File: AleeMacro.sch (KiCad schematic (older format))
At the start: 50 parts, among them J1 Conn_01x04_Male (OLED), SW1 SW_Push, U1 ProMicro

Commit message: Routing Adjustments
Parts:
- renumbered MX15a to MX16a1, MX19 to MX18a1
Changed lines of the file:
@@
 EESchema Schematic File Version 4
+LIBS:AleeMacro-cache
 EELAYER 30 0
 EELAYER END
@@
 	8525 5175 7925 5175
 $Comp
-L MX_Alps_Hybrids:MX-1U MX19
+L MX_Alps_Hybrids:MX-1U MX18a1
 U 1 1 5C43AB0B
 P 9725 4800
-F 0 "MX19" H 9811 5017 60  0000 C CNN
+F 0 "MX18a1" H 9811 5017 60  0000 C CNN
 F 1 "MX-2U" H 9811 4943 20  0000 C CNN
 F 2 "MX_Alps_Hybrid:MX-2U-ReversedStabilizers-NoLED" H 9700 4775 60  0001 C CNN
@@
 $EndComp
 $Comp
-L MX_Alps_Hybrids:MX-1U MX15a
+L MX_Alps_Hybrids:MX-1U MX16a1
 U 1 1 5C43B474
 P 8025 5550
-F 0 "MX15a" H 8111 5767 60  0000 C CNN
+F 0 "MX16a1" H 8111 5767 60  0000 C CNN
 F 1 "MX-2U" H 8111 5693 20  0000 C CNN
 F 2 "MX_Alps_Hybrid:MX-2U-ReversedStabilizers-NoLED" H 8000 5525 60  0001 C CNN

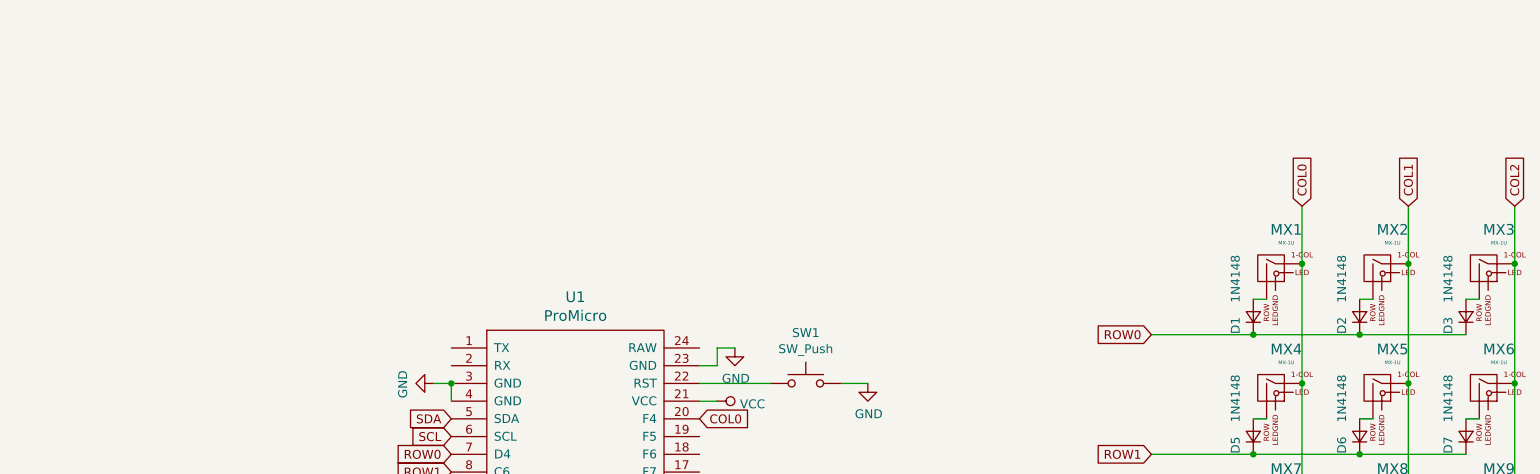
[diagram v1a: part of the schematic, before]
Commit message: LEDS added
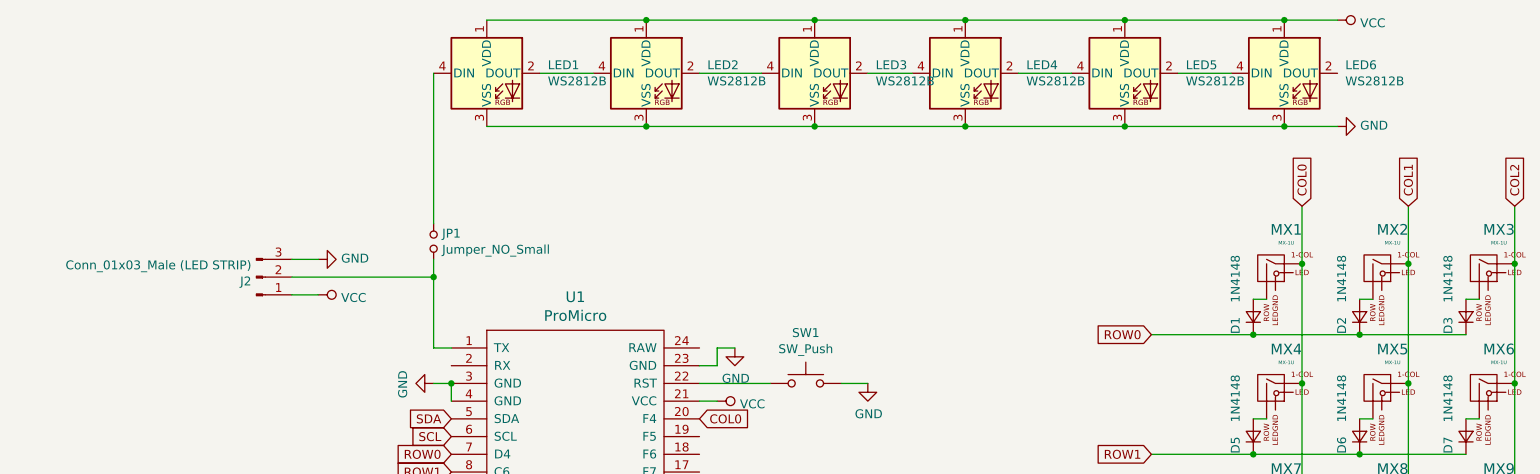
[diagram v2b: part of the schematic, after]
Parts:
- added J2: Conn_01x03_Male (LED STRIP), Connector_PinHeader_2.54mm:PinHeader_1x03_P2.54mm_Vertical, symbol Connector:Conn_01x03_Male
- added JP1: Jumper_NO_Small, Jumper:SolderJumper-2_P1.3mm_Open_Pad1.0x1.5mm, symbol Device:Jumper_NO_Small
- added LED1, LED2, LED3, LED4, LED5, LED6: WS2812B, LED_SMD:LED_WS2812B_PLCC4_5.0x5.0mm_P3.2mm, symbol LED:WS2812B
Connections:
- net GND: now also J2.3 (Pin_3), LED1.3 (VSS), LED2.3 (VSS), LED3.3 (VSS), LED4.3 (VSS), LED5.3 (VSS), LED6.3 (VSS)
- net VCC: now also J2.1 (Pin_1), LED1.1 (VDD), LED2.1 (VDD), LED3.1 (VDD), LED4.1 (VDD), LED5.1 (VDD), LED6.1 (VDD)
- net at U1.1 (TX): now also J2.2 (Pin_2), JP1.2
- new net: LED1.2 (DOUT), LED2.4 (DIN)
- new net: JP1.1, LED1.4 (DIN)
- new net: LED2.2 (DOUT), LED3.4 (DIN)
- new net: LED3.2 (DOUT), LED4.4 (DIN)
- new net: LED4.2 (DOUT), LED5.4 (DIN)
- new net: LED5.2 (DOUT), LED6.4 (DIN)
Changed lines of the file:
@@
 Wire Wire Line
 	4200 2850 4300 2850
+$Comp
+L power:GND #PWR0109
+U 1 1 6125BC2F
+P 7800 1300
+F 0 "#PWR0109" H 7800 1050 50  0001 C CNN
+F 1 "GND" V 7805 1172 50  0000 R CNN
+F 2 "" H 7800 1300 50  0001 C CNN
+F 3 "" H 7800 1300 50  0001 C CNN
+	1    7800 1300
+	0    -1   -1   0
+$EndComp
+$Comp
+L LED:WS2812B LED1
+U 1 1 61219799
+P 3000 1000
+F 0 "LED1" H 3344 1046 50  0000 L CNN
+F 1 "WS2812B" H 3344 955 50  0000 L CNN
+F 2 "LED_SMD:LED_WS2812B_PLCC4_5.0x5.0mm_P3.2mm" H 3050 700 50  0001 L TNN
+F 3 "https://cdn-shop.adafruit.com/datasheets/WS2812B.pdf" H 3100 625 50  0001 L TNN
+	1    3000 1000
+	1    0    0    -1
+$EndComp
+Wire Wire Line
+	2700 2550 2800 2550
+$Comp
+L LED:WS2812B LED4
+U 1 1 61284E59
+P 5700 1000
+F 0 "LED4" H 6044 1046 50  0000 L CNN
+F 1 "WS2812B" H 6044 955 50  0000 L CNN
+F 2 "LED_SMD:LED_WS2812B_PLCC4_5.0x5.0mm_P3.2mm" H 5750 700 50  0001 L TNN
+F 3 "https://cdn-shop.adafruit.com/datasheets/WS2812B.pdf" H 5800 625 50  0001 L TNN
+	1    5700 1000
+	1    0    0    -1
+$EndComp
+$Comp
+L LED:WS2812B LED5
+U 1 1 612874EB
+P 6600 1000
+F 0 "LED5" H 6944 1046 50  0000 L CNN
+F 1 "WS2812B" H 6944 955 50  0000 L CNN
+F 2 "LED_SMD:LED_WS2812B_PLCC4_5.0x5.0mm_P3.2mm" H 6650 700 50  0001 L TNN
+F 3 "https://cdn-shop.adafruit.com/datasheets/WS2812B.pdf" H 6700 625 50  0001 L TNN
+	1    6600 1000
+	1    0    0    -1
+$EndComp
+$Comp
+L LED:WS2812B LED6
+U 1 1 61289AF9
+P 7500 1000
+F 0 "LED6" H 7844 1046 50  0000 L CNN
+F 1 "WS2812B" H 7844 955 50  0000 L CNN
+F 2 "LED_SMD:LED_WS2812B_PLCC4_5.0x5.0mm_P3.2mm" H 7550 700 50  0001 L TNN
+F 3 "https://cdn-shop.adafruit.com/datasheets/WS2812B.pdf" H 7600 625 50  0001 L TNN
+	1    7500 1000
+	1    0    0    -1
+$EndComp
+Wire Wire Line
+	3300 1000 3600 1000
+Wire Wire Line
+	3000 1300 3900 1300
+$Comp
+L LED:WS2812B LED2
+U 1 1 6122436D
+P 3900 1000
+F 0 "LED2" H 4244 1046 50  0000 L CNN
+F 1 "WS2812B" H 4244 955 50  0000 L CNN
+F 2 "LED_SMD:LED_WS2812B_PLCC4_5.0x5.0mm_P3.2mm" H 3950 700 50  0001 L TNN
+F 3 "https://cdn-shop.adafruit.com/datasheets/WS2812B.pdf" H 4000 625 50  0001 L TNN
+	1    3900 1000
+	1    0    0    -1
+$EndComp
+$Comp
+L power:VCC #PWR0110
+U 1 1 61255F21
+P 7800 700
+F 0 "#PWR0110" H 7800 550 50  0001 C CNN
+F 1 "VCC" V 7817 828 50  0000 L CNN
+F 2 "" H 7800 700 50  0001 C CNN
+F 3 "" H 7800 700 50  0001 C CNN
+	1    7800 700
+	0    1    1    0
+$EndComp
+Wire Wire Line
+	3000 700  3900 700
+Connection ~ 3900 700
+Wire Wire Line
+	5700 700  6600 700
+Connection ~ 5700 700
+Wire Wire Line
+	6600 700  7500 700
+Connection ~ 6600 700
+Wire Wire Line
+	7500 700  7800 700
+Connection ~ 7500 700
+$Comp
+L LED:WS2812B LED3
+U 1 1 6128279B
+P 4850 1000
+F 0 "LED3" H 5194 1046 50  0000 L CNN
+F 1 "WS2812B" H 5194 955 50  0000 L CNN
+F 2 "LED_SMD:LED_WS2812B_PLCC4_5.0x5.0mm_P3.2mm" H 4900 700 50  0001 L TNN
+F 3 "https://cdn-shop.adafruit.com/datasheets/WS2812B.pdf" H 4950 625 50  0001 L TNN
+	1    4850 1000
+	1    0    0    -1
+$EndComp
+Wire Wire Line
+	3900 700  4850 700
+Connection ~ 4850 700
+Wire Wire Line
+	4850 700  5700 700
+Wire Wire Line
+	4200 1000 4550 1000
+Wire Wire Line
+	5150 1000 5400 1000
+Wire Wire Line
+	6000 1000 6300 1000
+Wire Wire Line
+	6900 1000 7200 1000
+Wire Wire Line
+	3900 1300 4850 1300
+Connection ~ 3900 1300
+Wire Wire Line
+	4850 1300 5700 1300
+Connection ~ 4850 1300
+Wire Wire Line
+	5700 1300 6600 1300
+Connection ~ 5700 1300
+Wire Wire Line
+	6600 1300 7500 1300
+Connection ~ 6600 1300
+Wire Wire Line
+	7500 1300 7800 1300
+Connection ~ 7500 1300
+$Comp
+L power:VCC #PWR0112
+U 1 1 612EDCFF
+P 2050 2250
+F 0 "#PWR0112" H 2050 2100 50  0001 C CNN
+F 1 "VCC" V 2067 2378 50  0000 L CNN
+F 2 "" H 2050 2250 50  0001 C CNN
+F 3 "" H 2050 2250 50  0001 C CNN
+	1    2050 2250
+	0    1    1    0
+$EndComp
+$Comp
+L Connector:Conn_01x03_Male J2
+U 1 1 612F1FD3
+P 1700 2150
+F 0 "J2" H 1672 2174 50  0000 R CNN
+F 1 "Conn_01x03_Male (LED STRIP)" H 1672 2083 50  0000 R CNN
+F 2 "Connector_PinHeader_2.54mm:PinHeader_1x03_P2.54mm_Vertical" H 1700 2150 50  0001 C CNN
+F 3 "~" H 1700 2150 50  0001 C CNN
+	1    1700 2150
+	1    0    0    1
+$EndComp
+Wire Wire Line
+	2700 2150 1900 2150
+Wire Wire Line
+	2050 2250 1900 2250
+Wire Wire Line
+	2050 2050 1900 2050
+$Comp
+L power:GND #PWR0111
+U 1 1 612EDCF9
+P 2050 2050
+F 0 "#PWR0111" H 2050 1800 50  0001 C CNN
+F 1 "GND" V 2055 1922 50  0000 R CNN
+F 2 "" H 2050 2050 50  0001 C CNN
+F 3 "" H 2050 2050 50  0001 C CNN
+	1    2050 2050
+	0    -1   -1   0
+$EndComp
+Wire Wire Line
+	2700 2150 2700 2550
+$Comp
+L Device:Jumper_NO_Small JP1
+U 1 1 612EBB5E
+P 2700 1950
+F 0 "JP1" V 2654 1998 50  0000 L CNN
+F 1 "Jumper_NO_Small" V 2745 1998 50  0000 L CNN
+F 2 "Jumper:SolderJumper-2_P1.3mm_Open_Pad1.0x1.5mm" H 2700 1950 50  0001 C CNN
+F 3 "~" H 2700 1950 50  0001 C CNN
+	1    2700 1950
+	0    1    1    0
+$EndComp
+Wire Wire Line
+	2700 2050 2700 2150
+Connection ~ 2700 2150
+Wire Wire Line
+	2700 1850 2700 1000
 $EndSCHEMATC
